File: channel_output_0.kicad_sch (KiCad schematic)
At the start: 33 parts, among them IC4 AP64501QSP-13, J9 Conn_01x02, U7 MCP4725xxx-xCH

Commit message: Added new DC/DC converter design
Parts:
- C29: footprint Hardware Components Footprints:C_0603_1608Metric -> Capacitor_SMD:C_0603_1608Metric
- C33, C49: footprint Hardware Components Footprints:C_0402_1005Metric -> Capacitor_SMD:C_0402_1005Metric
- R32, R4: footprint Hardware Components Footprints:R_0402_1005Metric -> Resistor_SMD:R_0402_1005Metric
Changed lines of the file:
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@@
 			)
 		)
-		(property "Footprint" "Hardware Components Footprints:C_0402_1005Metric"
+		(property "Footprint" "Capacitor_SMD:C_0402_1005Metric"
 			(at 132.08 66.04 0)
 			(effects
@@
 			)
 		)
-		(property "Footprint" "Hardware Components Footprints:R_0402_1005Metric"
+		(property "Footprint" "Resistor_SMD:R_0402_1005Metric"
 			(at 154.94 62.23 0)
 			(effects
@@
 			)
 		)
-		(property "Footprint" "Hardware Components Footprints:C_0603_1608Metric"
+		(property "Footprint" "Capacitor_SMD:C_0603_1608Metric"
 			(at 152.4 69.85 0)
 			(effects
@@
 			)
 		)
-		(property "Footprint" "Hardware Components Footprints:R_0402_1005Metric"
+		(property "Footprint" "Resistor_SMD:R_0402_1005Metric"
 			(at 118.11 46.99 0)
 			(effects
@@
 			)
 		)
-		(property "Footprint" "Hardware Components Footprints:C_0402_1005Metric"
+		(property "Footprint" "Capacitor_SMD:C_0402_1005Metric"
 			(at 161.29 71.12 0)
 			(effects

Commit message: Update inductor
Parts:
- L4: footprint Inductor_SMD:L_Bourns_SRR1210A -> Inductor_SMD:L_Wuerth_XHMI-6060; ISat 6.5A -> 9.9A; MPN SRR1210A-100M -> 744393465100; Manufacturer Coilcraft -> Wuerth
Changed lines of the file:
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@@
 			)
 		)
-		(property "Footprint" "Inductor_SMD:L_Bourns_SRR1210A"
+		(property "Footprint" "Inductor_SMD:L_Wuerth_XHMI-6060"
 			(at 165.1 78.74 0)
 			(effects
@@
 			)
 		)
-		(property "Datasheet" "https://www.mouser.pl/datasheet/3/40/1/SRR1210A.pdf"
+		(property "Datasheet" "https://www.we-online.com/components/products/datasheet/744393465100.pdf"
 			(at 165.1 81.28 0)
 			(effects
@@
 			)
 		)
-		(property "Description" "Power Inductor (SMD), 10 µH, 6.5 A, Shielded"
+		(property "Description" "Power Inductor (SMD),  10uH 10A, Shielded"
 			(at 149.86 66.04 0)
 			(effects
@@
 			)
 		)
-		(property "Manufacturer" "Coilcraft"
+		(property "Manufacturer" "Wuerth"
 			(at 165.1 83.82 0)
 			(effects
@@
 			)
 		)
-		(property "MPN" " SRR1210A-100M "
+		(property "MPN" "744393465100"
 			(at 165.1 86.36 0)
 			(effects
@@
 			)
 		)
-		(property "ISat" "6.5A"
+		(property "ISat" "9.9A"
 			(at 165.1 88.9 0)
 			(effects

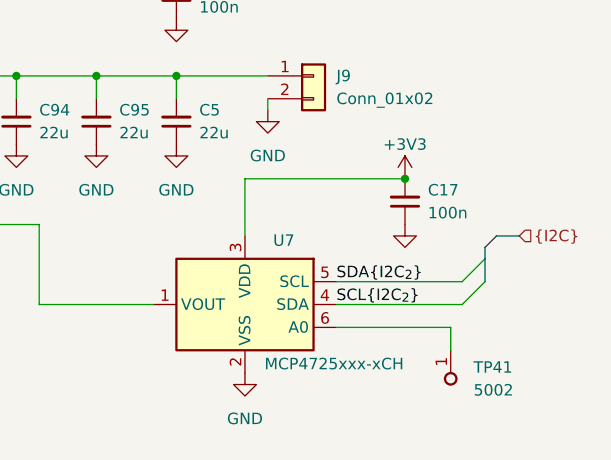
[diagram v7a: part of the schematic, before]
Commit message: Layout I2C not connected
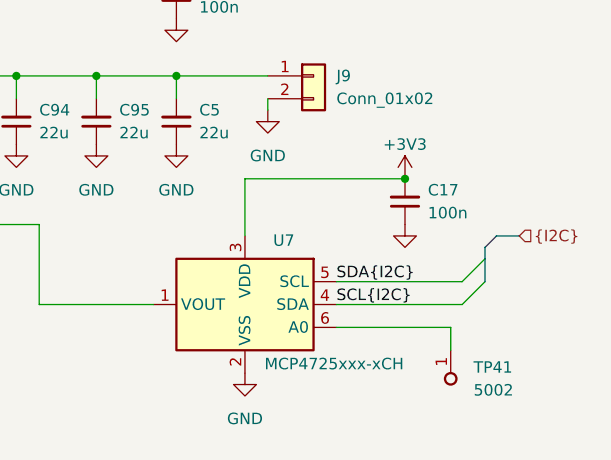
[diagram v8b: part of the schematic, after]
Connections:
- net GND: now also IC4.9 (GND)
- net SCL{I2C_{2}} renamed SCL{I2C}
- net SDA{I2C_{2}} renamed SDA{I2C}
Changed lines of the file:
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@@
 		)
 	)
-	(label "SDA{I2C_{2}}"
+	(label "SDA{I2C}"
 		(at 223.52 88.9 0)
 		(effects
@@
 		)
 	)
-	(label "SCL{I2C_{2}}"
+	(label "SCL{I2C}"
 		(at 223.52 91.44 0)
 		(effects
@@
 		(pin "8"
 		)
-		(pin "7"
+		(pin "9"
 		)
 		(pin "1"
@@
 		(pin "4"
 		)
+		(pin "7"
+		)
 		(instances
